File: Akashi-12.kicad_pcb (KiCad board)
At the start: 2 copper layers, 30 parts, among them J1 USB Type-C receptacle, SW1 SW_MEC_5E, SW2 SW_MEC_5E, U1 IC57_RP2040, U2 W25Q32JVSS, U3 NCP1117-3.3_SOT223, Y1 12MHz

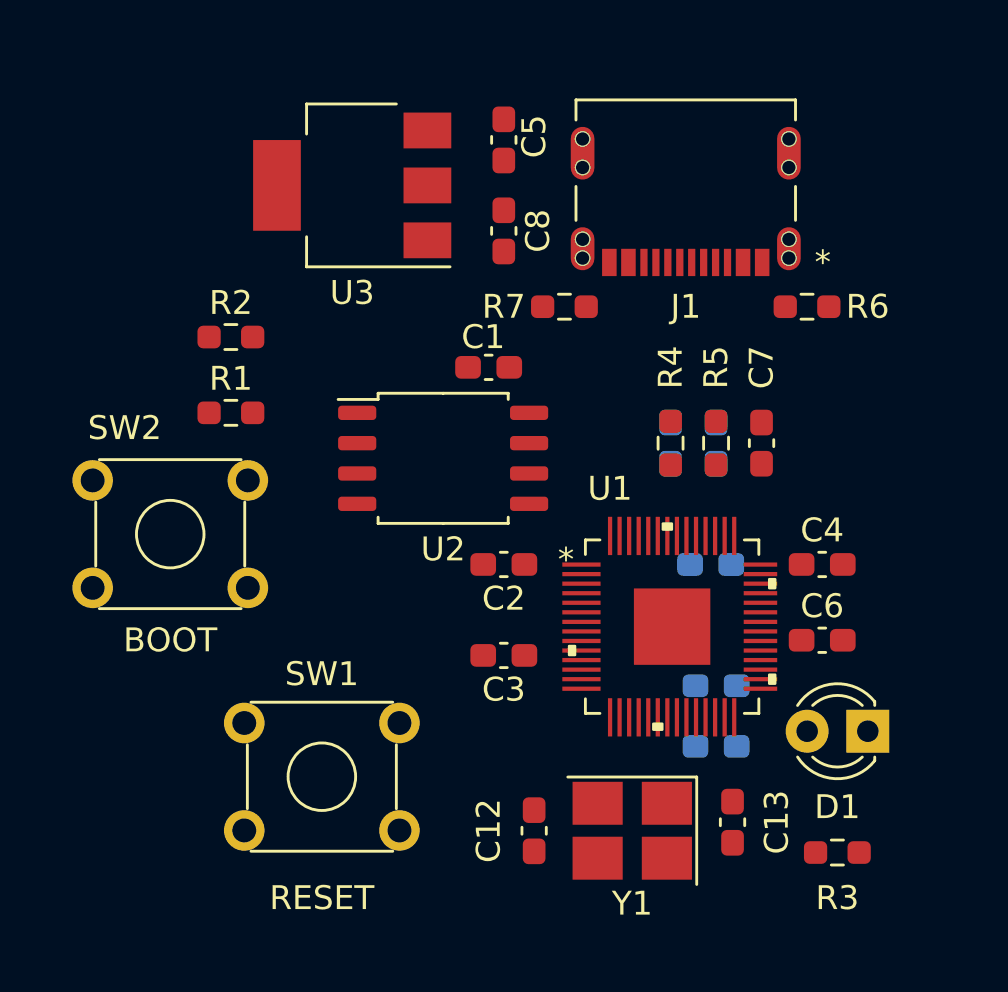
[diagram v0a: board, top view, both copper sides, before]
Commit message: Update layout and USB connector footpring
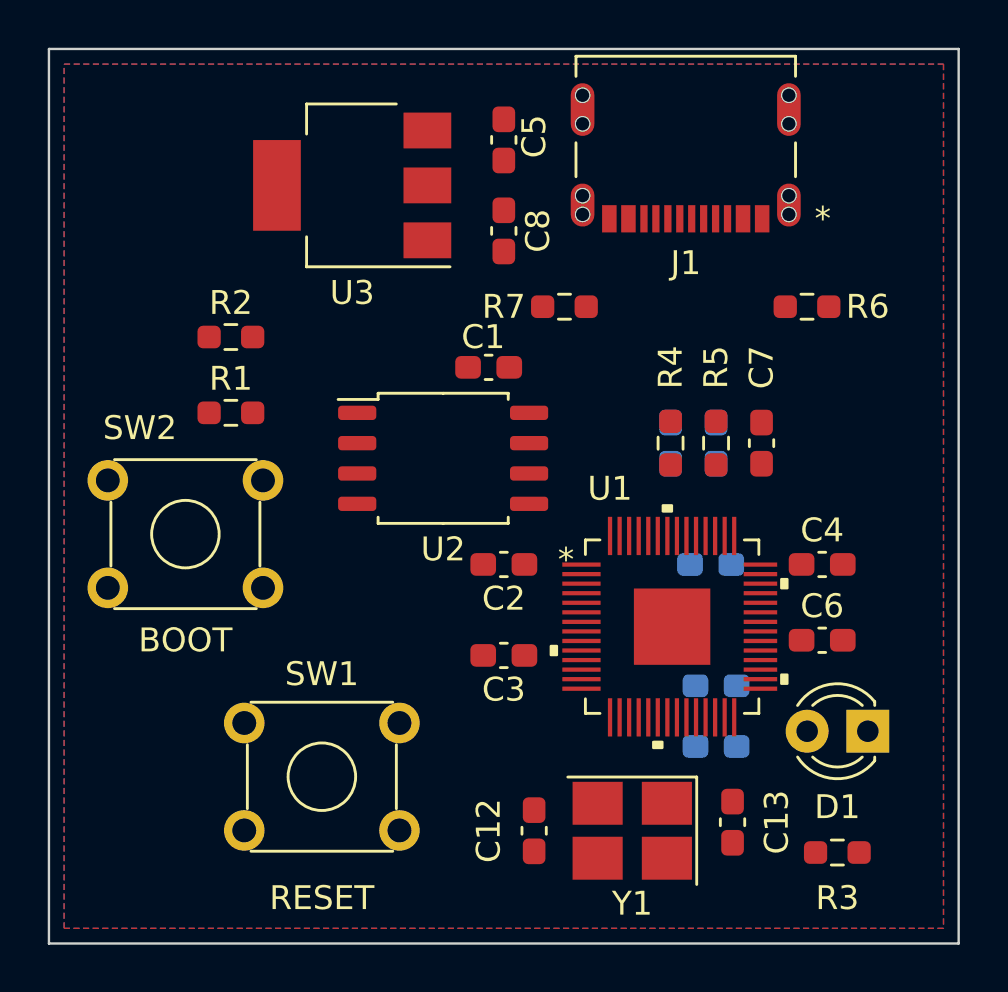
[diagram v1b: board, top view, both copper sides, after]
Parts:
- moved J1 1.83 mm to (166.4, 94.6)
- moved SW2 0.63 mm to (148.7, 113.4)
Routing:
- added copper zone on F.Cu, net +3V3
- added copper zone on B.Cu, net GND
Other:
- board outline added: 38.1 x 37.5 mm
